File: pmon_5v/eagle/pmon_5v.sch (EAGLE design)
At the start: 30 parts, among them J1 USB, J2 USB, J4 USB_A, J5 PINHD-2X3, Q1 16Mhz, U1 LTC2943, U2 FT232RL, U4 ATMEGA328TQFP32

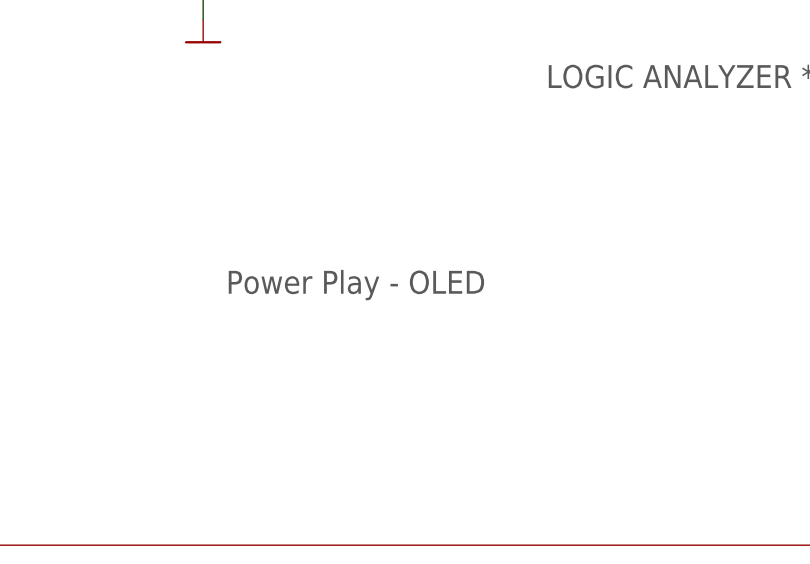
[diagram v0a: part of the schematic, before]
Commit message: Added pdf dumps of board and schematic.
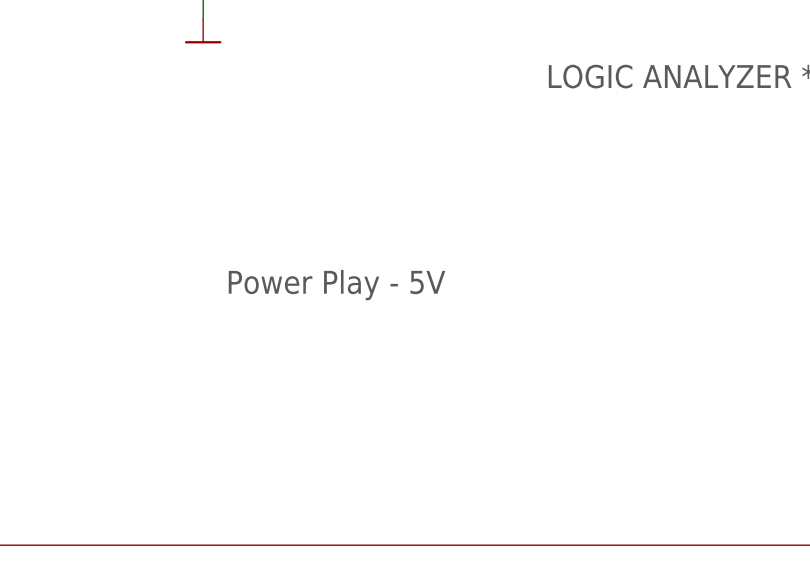
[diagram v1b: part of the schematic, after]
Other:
- note added: "Power Play - 5V"
- note removed: "Power Play - OLED"
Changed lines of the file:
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@@
 <text x="204.47" y="104.14" size="2.54" layer="97">ICSP (POGO)</text>
 <text x="210.82" y="146.05" size="2.54" layer="97">MCU</text>
-<text x="185.42" y="27.94" size="2.54" layer="97" font="vector">Power Play - OLED</text>
+<text x="185.42" y="27.94" size="2.54" layer="97" font="vector">Power Play - 5V</text>
 <wire x1="-35.56" y1="238.76" x2="281.94" y2="238.76" width="0.1524" layer="94"/>
 <wire x1="281.94" y1="238.76" x2="281.94" y2="0" width="0.1524" layer="94"/>

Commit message: Cleaned up the board.
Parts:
- removed C12: 20pF, pmon_5v:CAP-C0603
- removed J5: PINHD-2X3, pmon_5v:PINHD-2X3
- added C8: 0.1uF, pmon_5v:CAP-C0603
- added J3: USB_A, pmon_5v:USB_A
- C10: value 0.1uF -> 20pF
- C3: value 10uF -> 0.1uF; device pmon_5v:CPOL-USA/3216-18R -> pmon_5v:CAP-C0603
- C4: value 0.1uF -> 10uF; device pmon_5v:CAP-C0603 -> pmon_5v:CPOL-USA/3216-18R
- J4: value USB_A -> PINHD-2X3; device pmon_5v:USB_A -> pmon_5v:PINHD-2X3
- R4: value 10K -> 0.025R 1%; device pmon_5v:RES-R0603 -> pmon_5v:RES-SHUNT-6432
- R6: value 0.025R 1% -> 10K; device pmon_5v:RES-SHUNT-6432 -> pmon_5v:RES-R0603
- renumbered C11 to C9, R10 to R7, R11 to R8, U4 to U3
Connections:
- net +5V: now also C4.+, C5.1, C8.1, J2.VBUS, J4.2, R4.I2; no longer C10.1, C3.+, C4.1, J1.VBUS, J5.2, R6.I2
- net GND: now also C3.2, C4.-, C8.2, J3.(-), J4.6; no longer C12.2, C3.-, C4.2, J4.(-), J5.6
- net MISO: now also J4.1; no longer J5.1
- net MOSI: now also J4.4; no longer J5.4
- net N$10: now also J1.D+; no longer J2.D+
- net N$15: now also J1.D-; no longer J2.D-
- net N$22: now also J3.(+), R4.I1; no longer J4.(+), R6.I1
- net N$4: now also J3.D+, J3.D-; no longer J4.D+, J4.D-
- net N$6: now also R5.2; no longer R4.2
- net N$7: now also C10.1; no longer C12.1
- net N$8: now also R6.2; no longer R5.2
- net RESET: now also J4.5; no longer J5.5
- net SCK: now also J4.3; no longer J5.3
- net SENSE+: now also R4.V2; no longer R6.V2
- net SENSE-: now also R4.V1; no longer R6.V1
- net SER_RX: now also R5.1; no longer R4.1
- net SER_TX: now also R6.1; no longer R5.1
- net VUSB: now also C3.1, J1.VBUS; no longer C5.1, J2.VBUS
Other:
- moved on the sheet: C10, C5, J1, J2, R5
